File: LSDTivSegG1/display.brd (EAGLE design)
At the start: 150 x 100 mm, 123 parts, among them IC1 MEGA8-P, IC2 MAX232, IC3 PCF8574P, IC4 PCF8574P, IC5 PCF8574P, IC6 PCF8574P, T1 BC847, T10 BC847, T11 BC847, T12 BC847, T13 BC847, T14 BC847, T15 BC847, T16 BC847, T17 BC847, T18 BC847, T19 BC847, T2 BC847, T20 BC847, T21 BC847, T22 BC847, T23 BC847, T24 BC847, T3 BC847, T4 BC847, T5 BC847, T6 BC847, T7 BC847, T8 BC847, T9 BC847

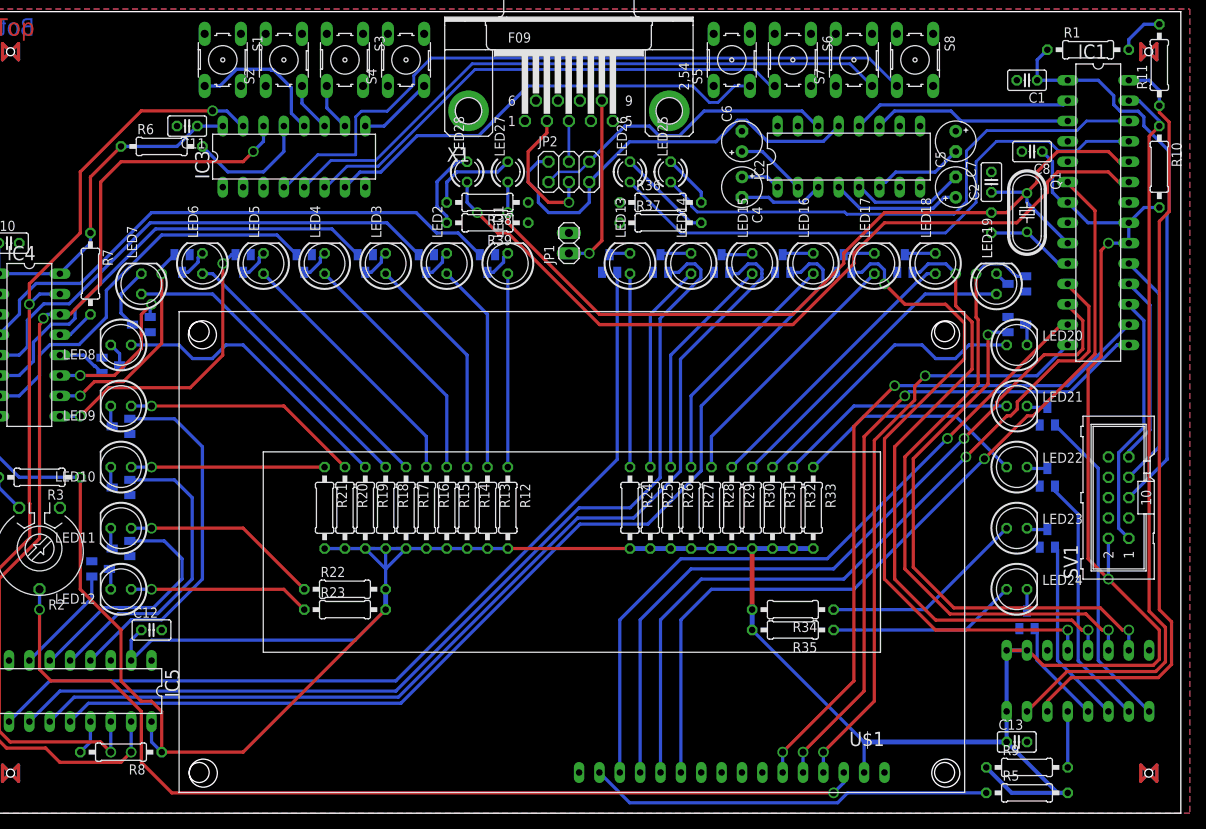
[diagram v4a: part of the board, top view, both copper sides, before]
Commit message: finished routing there just some wire stubs to remove (DRC)
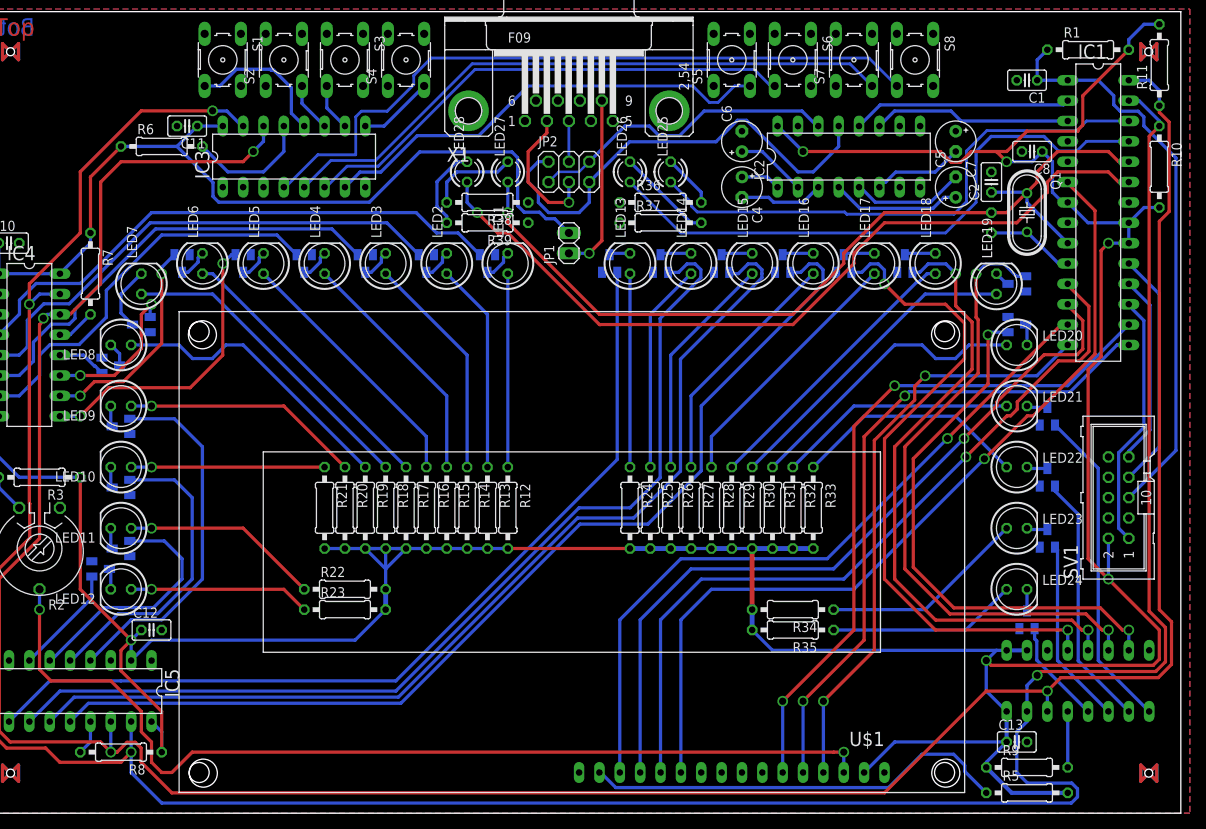
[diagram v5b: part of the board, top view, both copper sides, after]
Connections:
- net BTN0: no longer S8.3
- net BTN1: no longer S7.4
- net BTN2: no longer S6.3
- net BTN3: no longer S5.4
- net BTN4: no longer S4.4
- net BTN5: no longer S3.3
- net BTN6: no longer S2.4
- net BTN7: no longer S1.3
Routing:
- net SDA: track 221.0 -> 362.9 mm, vias 3 -> 4
- net SCL: track 214.2 -> 341.1 mm, vias 3 -> 4
- net +5V: track 491.1 -> 575.4 mm, vias 2 -> 6
- net RS232TX: track 53.5 -> 58.2 mm
- net N$11: track 50.3 -> 53.2 mm
- net N$42: track 73.6 -> 74.8 mm
- net RESET: track 71.2 -> 71.8 mm

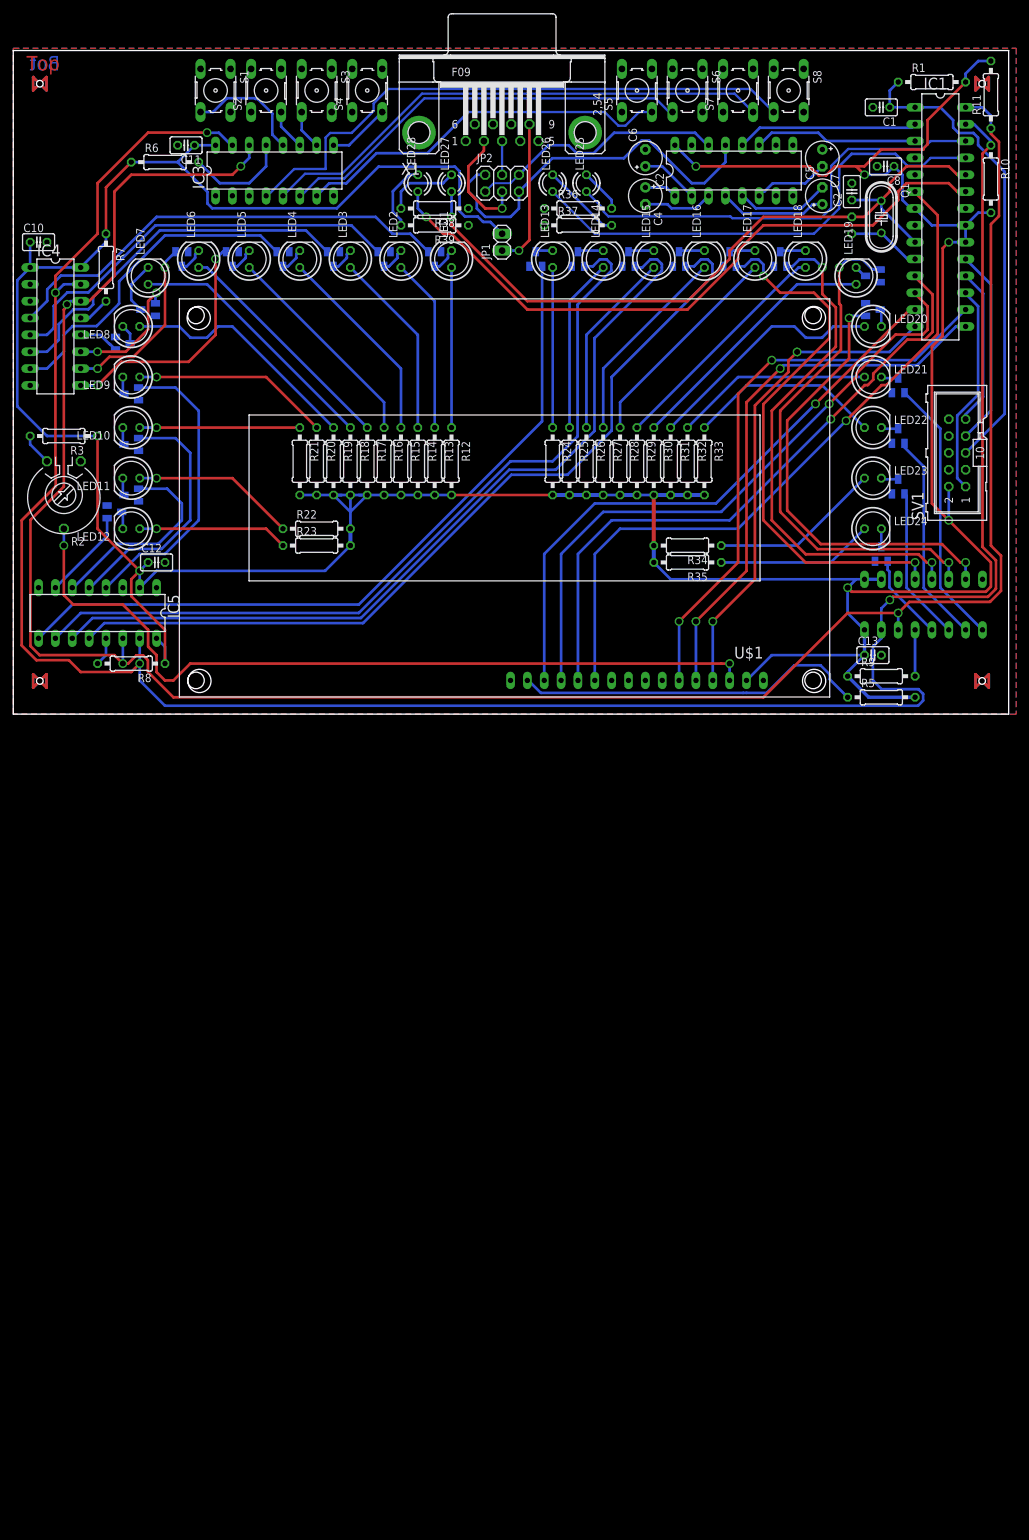
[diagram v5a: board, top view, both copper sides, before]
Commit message: removed wire stub drc warnings, increased wire width for +5V
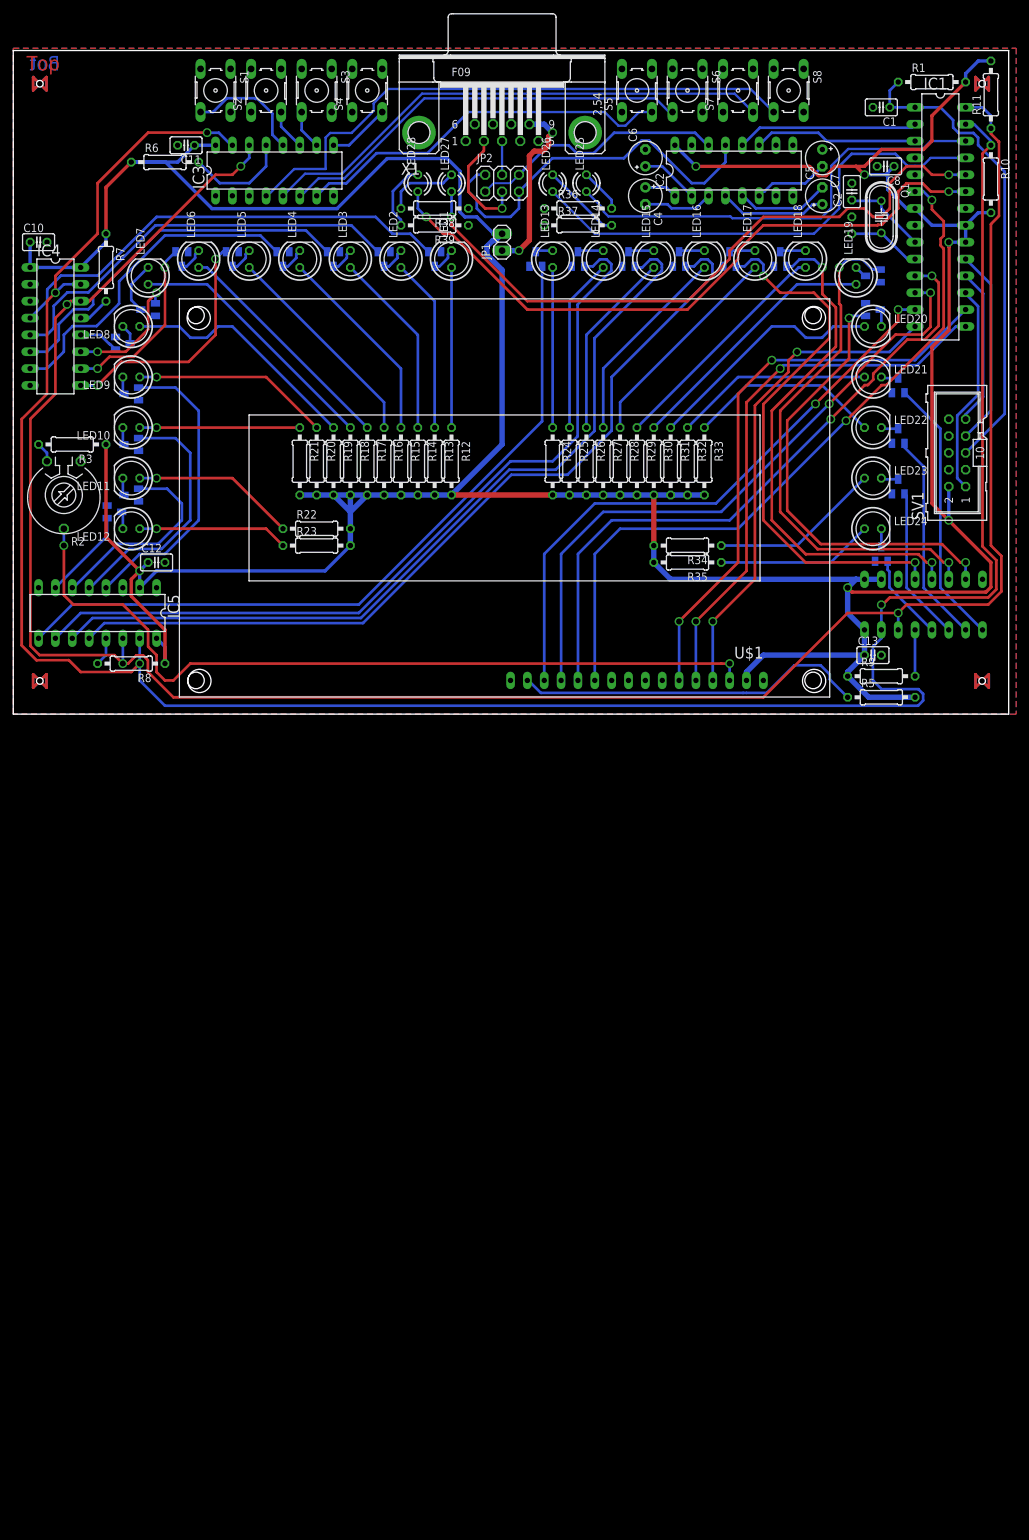
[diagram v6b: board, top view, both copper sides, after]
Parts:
- moved R3 1.80 mm to (8.89, 40.6)
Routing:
- net +5V: track 575.4 -> 586.7 mm
- net N$48: track 22.2 -> 27.2 mm, vias 1 -> 2
- net SCL: track 341.1 -> 336.8 mm
- net N$41: track 97.7 -> 100.3 mm, vias 1 -> 2
- net D5: track 96.4 -> 98.7 mm, vias 1 -> 2
- net D4: track 107.3 -> 109.2 mm, vias 1 -> 2
- net N$9: track 4.86 -> 3.07 mm
- net D6: track 94.9 -> 96.6 mm, vias 1 -> 2
- net D7: track 90.2 -> 91.2 mm, vias 1 -> 2
- net N$40: track 101.3 -> 102.1 mm, vias 1 -> 2
